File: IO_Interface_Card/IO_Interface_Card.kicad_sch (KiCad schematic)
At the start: 97 parts, among them P1 Conn_02x40_Odd_Even, P2 Conn_02x36_Top_Bottom

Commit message: Finished Adding Every Chip and Net label in AU1
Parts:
- removed E26, E27: Terminal, Connector_PinHeader_2.54mm:PinHeader_1x01_P2.54mm_Horizontal, symbol Connector_Generic:Conn_01x01
- E1, E10, E11, E12, E13, E14, E15, E16, E17, E18, E19, E2, E20, E21, E22, E23, E24, E25, E26, E27, E28, E29, E3, E30, E31, E32, E33, E34, E35, E36, E37, E38, E39, E4, E40, E41, E42, E43, E44, E45, E46, E47, E5, E6, E7, E8, E9: footprint Connector_PinHeader_2.54mm:PinHeader_1x01_P2.54mm_Horizontal -> Connector_PinHeader_2.54mm:PinHeader_1x01_P2.54mm_Vertical
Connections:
- net IOUT5A: now also Z9.2 (~{R})
- net IOUT6A: now also Z9.1 (CLK)

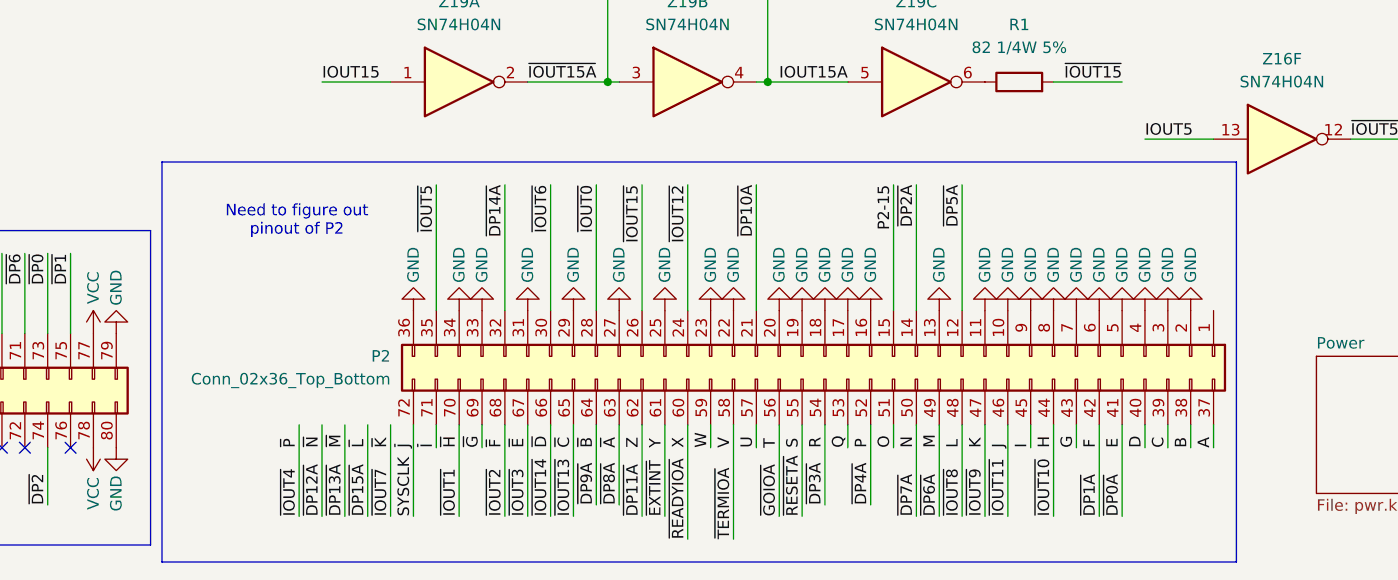
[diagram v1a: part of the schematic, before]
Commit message: Updated Schematic on IO Interface card and Made Schematic for IO Extender 1 Card
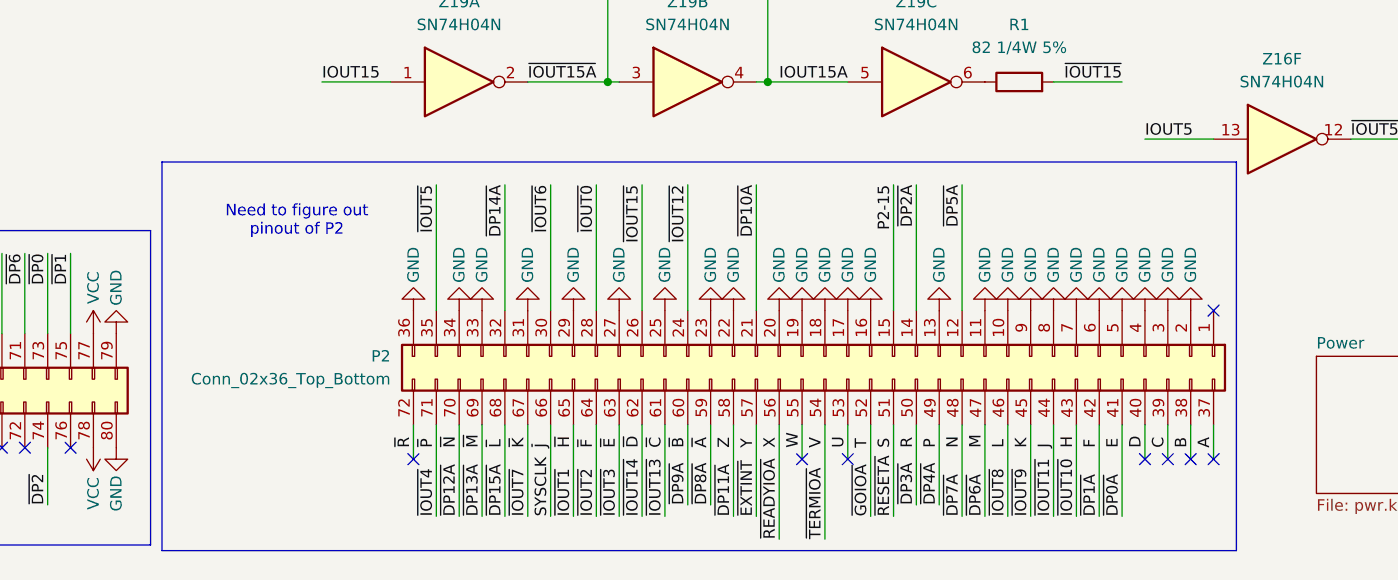
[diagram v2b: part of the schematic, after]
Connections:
- net G is gone; now on net H: P2.43 (Pin_43)
- net I is gone; now on net K: P2.45 (Pin_45)
- net O is gone; now on net S: P2.51 (Pin_51)
- net Q is gone; now on net U: P2.53 (Pin_53)
- net ~{G} is gone; now on net ~{DP13A}: P2.69 (Pin_69)
- net ~{I} is gone; now on net ~{IOUT4}: P2.71 (Pin_71)
- net H: no longer P2.44 (Pin_44)
- net J: now also P2.44 (Pin_44); no longer P2.46 (Pin_46)
- net K: no longer P2.47 (Pin_47)
- net L: now also P2.46 (Pin_46); no longer P2.48 (Pin_48)
- net M: now also P2.47 (Pin_47); no longer P2.49 (Pin_49)
- net N: now also P2.48 (Pin_48); no longer P2.50 (Pin_50)
- net P: now also P2.49 (Pin_49); no longer P2.52 (Pin_52)
- net R: now also P2.50 (Pin_50); no longer P2.54 (Pin_54)
- net S: no longer P2.55 (Pin_55)
- net SYSCLK: now also P2.66 (Pin_66); no longer P2.72 (Pin_72)
- net T: now also P2.52 (Pin_52); no longer P2.56 (Pin_56)
- net U: no longer P2.57 (Pin_57)
- net V: now also P2.54 (Pin_54); no longer P2.58 (Pin_58)
- net W: now also P2.55 (Pin_55); no longer P2.59 (Pin_59)
- net X: now also P2.56 (Pin_56); no longer P2.60 (Pin_60)
- net Y: now also P2.57 (Pin_57); no longer P2.61 (Pin_61)
- net Z: now also P2.58 (Pin_58); no longer P2.62 (Pin_62)
- net ~{A}: now also P2.59 (Pin_59); no longer P2.63 (Pin_63)
- net ~{B}: now also P2.60 (Pin_60); no longer P2.64 (Pin_64)
- net ~{C}: now also P2.61 (Pin_61); no longer P2.65 (Pin_65)
- net ~{DP12A}: now also P2.70 (Pin_70)
- net ~{DP15A}: now also P2.68 (Pin_68)
- net ~{D}: now also P2.62 (Pin_62); no longer P2.66 (Pin_66)
- net ~{E}: now also P2.63 (Pin_63); no longer P2.67 (Pin_67)
- net ~{F}: now also P2.64 (Pin_64); no longer P2.68 (Pin_68)
- net ~{H}: now also P2.65 (Pin_65); no longer P2.70 (Pin_70)
- net ~{IOUT7}: now also P2.67 (Pin_67)
- new net ~{R}: P2.72 (Pin_72)
- no-connect marks 33 -> 41
